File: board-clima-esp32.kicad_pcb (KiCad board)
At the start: 2 copper layers, 64.8 x 39.9 mm, 32 parts, among them IC1 ESP32-S3-WROOM-1-N4, J1 Conn_01x02_Pin, J2 Screw_Terminal_01x03, J3 Conn_01x04_Pin, J4 Conn_01x04_Pin, J5 Conn_01x04_Pin, J6 USB_C_Receptacle, Q1 AO3400A, SW1 RESET, SW2 BOOT, U1 AMS1117-3.3, U2 JZC-32F/C

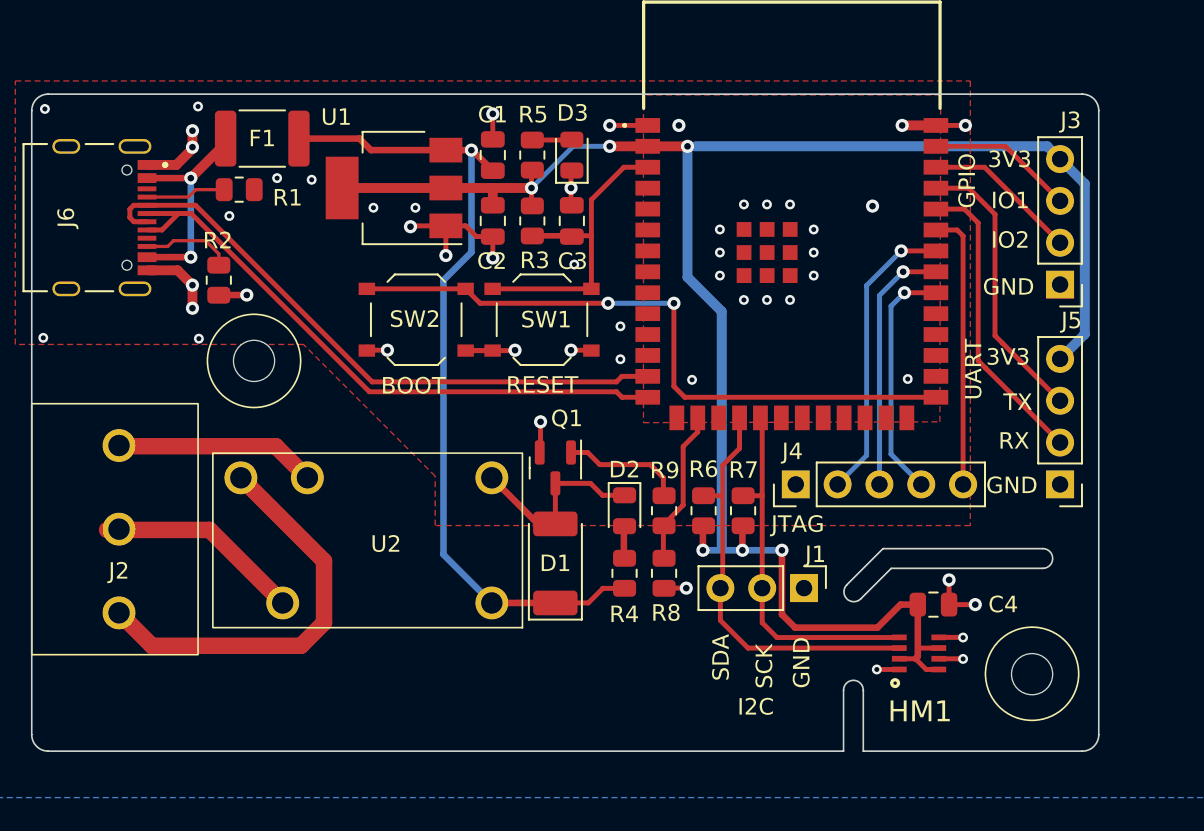
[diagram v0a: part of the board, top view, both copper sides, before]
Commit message: added bypass jumper
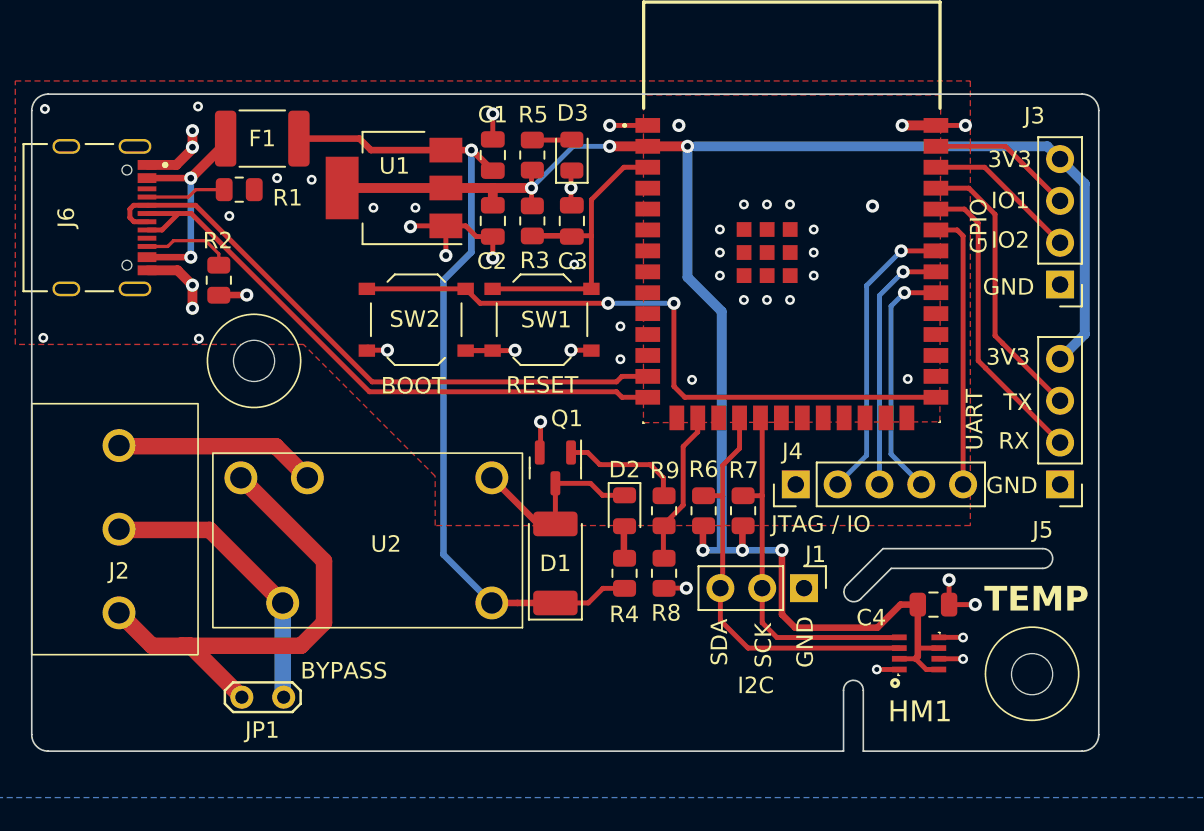
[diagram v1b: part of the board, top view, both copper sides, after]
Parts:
- added JP1: Jumper_2_Open, TestPoint:TestPoint_2Pads_Pitch2.54mm_Drill0.8mm, F.Cu at (106.3, 90.4)
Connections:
- net Net-(J2-Pin_1) renamed /R_NO
- net Net-(J2-Pin_2) renamed /R_COM
- J6 pad S1: unconnected-(J6-SHIELD-PadS1) -> GND
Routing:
- net /R_COM: track 12.5 -> 17.5 mm
- net /R_NO: track 24.8 -> 29.7 mm
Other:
- board text added: "BYPASS"
- board text added: "JTAG / IO"
- board text added: "TEMP"
- board text removed: "JTAG"

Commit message: pcb rev2 placement
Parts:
- removed J4: Conn_01x04_Pin, Connector_PinHeader_2.54mm:PinHeader_1x05_P2.54mm_Vertical
- added C5: 1u, Capacitor_SMD:C_0805_2012Metric, F.Cu at (159.8, 126.2)
- added D10: 15V, Diode_SMD:D_SOD-323, F.Cu at (169.2, 173.4)
- added D4: SM4007PL, Diode_SMD:D_SOD-123F, F.Cu at (160.0, 170.4)
- added D5: SM4007PL, Diode_SMD:D_SOD-123F, F.Cu at (163.3, 170.2)
- added D6: SM4007PL, Diode_SMD:D_SOD-123F, F.Cu at (160.0, 175.0)
- added D7: SM4007PL, Diode_SMD:D_SOD-123F, F.Cu at (163.3, 175.0)
- added D8: 4V3, Diode_SMD:D_SOD-323, F.Cu at (174.5, 176.5)
- added D9: 4V7, Diode_SMD:D_SOD-323, F.Cu at (169.2, 177.0)
- added H3: MountingHole, MountingHole:MountingHole_2.5mm, F.Cu at (130.3, 184.9)
- added H4: MountingHole, MountingHole:MountingHole_2.5mm, F.Cu at (200.7, 184.9)
- added Q2: AO3401A, Package_TO_SOT_SMD:SOT-23, F.Cu at (168.3, 169.9)
- added Q3: AO3400A, Package_TO_SOT_SMD:SOT-23, F.Cu at (165.6, 158.8)
- added R10: 10k, Resistor_SMD:R_0805_2012Metric, F.Cu at (170.2, 157.2)
- added R11: 330, Resistor_SMD:R_0805_2012Metric, F.Cu at (172.5, 169.2)
- added R12: 220, Resistor_SMD:R_0805_2012Metric, F.Cu at (166.9, 173.5)
- added R13: 100, Resistor_SMD:R_0805_2012Metric, F.Cu at (166.9, 177.0)
- added R14: 10k, Resistor_SMD:R_0805_2012Metric, F.Cu at (189.0, 179.1)
- added R15: 330, Resistor_SMD:R_0805_2012Metric, F.Cu at (189.0, 171.4)
- added R16: 220, Resistor_SMD:R_0805_2012Metric, F.Cu at (170.2, 165.4)
- added R17: 10k, Resistor_SMD:R_0805_2012Metric, F.Cu at (170.2, 163.1)
- added U3: PC817, Package_DIP:DIP-4_W7.62mm, F.Cu at (185.7, 172.2)
- added U4: PC817, Package_DIP:DIP-4_W7.62mm, F.Cu at (178.1, 176.5)
- D1: value SM4007 -> SM4007PL; footprint Diode_SMD:D_MELF -> Diode_SMD:D_SOD-123F
- D2: value LED -> SM4007PL; footprint LED_SMD:LED_0805_2012Metric -> Diode_SMD:D_SOD-123F
- J1: value Conn_01x02_Pin -> Conn_01x06_Pin; footprint Connector_PinHeader_2.54mm:PinHeader_1x03_P2.54mm_Vertical -> Connector_PinHeader_2.54mm:PinHeader_1x06_P2.54mm_Vertical
- J5: value Conn_01x04_Pin -> Conn_01x05_Pin; footprint Connector_PinHeader_2.54mm:PinHeader_1x04_P2.54mm_Vertical -> Connector_PinHeader_2.54mm:PinHeader_1x05_P2.54mm_Vertical
- R4: value 220 -> 0
- R5: value 220 -> 1k
- R8: value 10k -> 0
- U2: value JZC-32F/C -> ~; footprint JZC-32FC:JZC-32FC -> HFD2:HFD2-00X-M-L2
- moved C4 105.6 mm to (195.3, 178.1)
- moved J1 101.1 mm to (197.6, 165.4), turned to 180 degrees
- moved HM1 99.7 mm to (193.7, 176.2), turned to 90 degrees
- moved Q1 97.7 mm to (165.5, 164.3), turned to 180 degrees
- moved JP1 93.3 mm to (133.9, 179.6), turned to 90 degrees
- moved U2 90.9 mm to (157.1, 169.6)
- moved D1 90.3 mm to (160.4, 164.3), turned to -90 degrees
- moved R9 90.2 mm to (170.2, 159.5), turned to 0 degrees
- moved SW2 87.4 mm to (156.5, 144.1)
- moved R2 87.0 mm to (142.5, 142.2)
- moved D2 86.1 mm to (160.4, 158.5)
- moved J6 85.8 mm to (129.7, 138.9)
- moved R7 85.3 mm to (184.4, 148.1), turned to 0 degrees
- moved R6 84.9 mm to (184.4, 145.8), turned to 0 degrees
- moved R1 84.9 mm to (138.2, 137.2)
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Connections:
- D1 pad 1: +5V -> Net-(D1-K)
- D2 pad 1: Net-(D1-A) -> Net-(D2-K)
- IC1 pad 16: /RELAY -> unconnected-(IC1-IO46-Pad16)
- IC1 pad 18: /SDA -> /BOILER_1
- IC1 pad 19: /SCK -> /BOILER_2
- IC1 pad 21: unconnected-(IC1-IO13-Pad21) -> /GPIO4
- IC1 pad 22: unconnected-(IC1-IO14-Pad22) -> /GPIO5
- IC1 pad 23: unconnected-(IC1-IO21-Pad23) -> /SDA
- IC1 pad 24: unconnected-(IC1-IO47-Pad24) -> /SCK
- IC1 pad 31: unconnected-(IC1-IO38-Pad31) -> /GPIO3
- IC1 pad 32: /JTAG_TCK -> unconnected-(IC1-IO39-Pad32)
- IC1 pad 33: /JTAG_TDO -> unconnected-(IC1-IO40-Pad33)
- IC1 pad 34: /JTAG_TDI -> unconnected-(IC1-IO41-Pad34)
- IC1 pad 35: /JTAG_TMS -> unconnected-(IC1-IO42-Pad35)
- IC1 pad 38: /GPIO2 -> /GPIO1
- IC1 pad 39: /GPIO1 -> /GPIO2
- J1 pad 1: GND -> /GPIO5
- J1 pad 2: /SCK -> /GPIO4
- J2 pad 3: Net-(J2-Pin_3) -> /R_NC
- J5 pad 1: GND -> /GPIO3
- J5 pad 4: +3.3V -> GND
- R4 pad 2: Net-(D2-A) -> Net-(D1-K)
- R6 pad 2: /SDA -> /SCK
- R7 pad 2: /SCK -> /SDA
- R8 pad 1: /RELAY -> +5V
- R8 pad 2: GND -> Net-(D2-K)
- R9 pad 1: /RELAY -> /BOILER_2
- R9 pad 2: Net-(Q1-G) -> Net-(Q3-G)
- U2 pad 1: +5V -> Net-(D1-A)
- U2 pad 2: Net-(D1-A) -> Net-(D2-A)
- U2 pad 4: Net-(J2-Pin_3) -> /R_COM
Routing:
- net +3.3V: track 114.0 -> 0.00 mm, vias 6 -> 0
- net +5V: track 50.4 -> 0.00 mm, vias 1 -> 0
- net GND: track 46.3 -> 0.00 mm, vias 51 -> 0
- net /BOOT: track 39.8 -> 0.00 mm, vias 2 -> 0
- net /USB-: track 37.4 -> 0.00 mm
- net /USB+: track 36.8 -> 0.00 mm
- net /R_NO: track 29.7 -> 0.00 mm
- net /SDA: track 25.1 -> 0.00 mm
- net /SCK: track 22.5 -> 0.00 mm
- net Net-(IC1-EN): track 21.2 -> 0.00 mm
- net /UART_RX: track 18.8 -> 0.00 mm
- net /JTAG_TDI: track 17.9 -> 0.00 mm, vias 1 -> 0
- net /UART_TX: track 17.6 -> 0.00 mm
- net /R_COM: track 17.5 -> 0.00 mm
- net /JTAG_TMS: track 17.3 -> 0.00 mm
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- removed copper zone on B.Cu, net GND
- removed copper zone on F.Cu, net GND
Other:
- board size 64.8 x 39.9 mm -> 76.2 x 64.3 mm
- board text removed: "${COMMENT1}"
- board text removed: "${COMPANY} ${REVISION} NO WARRANTY WHATSOEVER USAGE AT USER'S OWN RISK"
- board text removed: "3V3"
- board text removed: "BOOT"
- board text removed: "BYPASS"
- board text removed: "GND"
- board text removed: "GPIO"
- board text removed: "I2C"
- board text removed: "IO1"
- board text removed: "IO2"
- board text removed: "JTAG / IO"
- board text removed: "RESET"
- board text removed: "RX"
- board text removed: "SCK"
- board text removed: "SDA"
- board text removed: "TEMP"
- board text removed: "TX"
- board text removed: "UART"

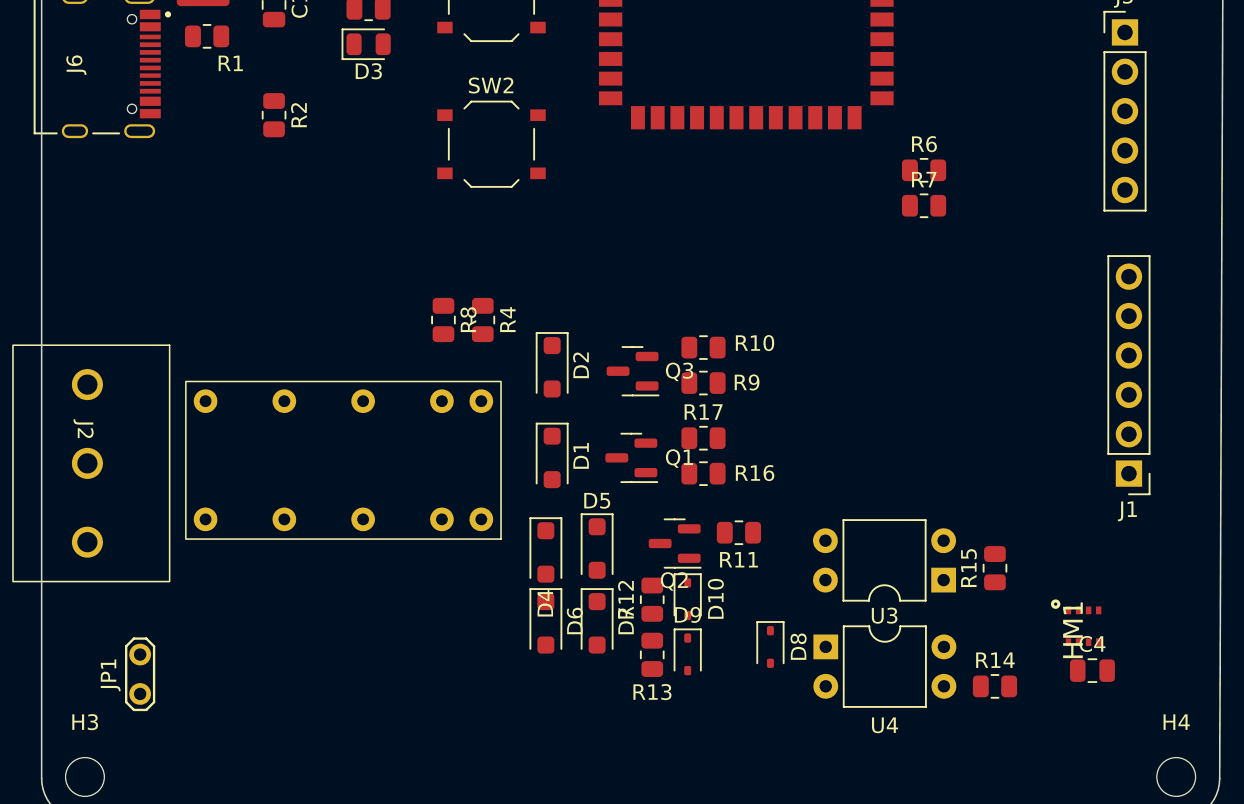
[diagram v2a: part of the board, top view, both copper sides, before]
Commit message: New J1 connector location
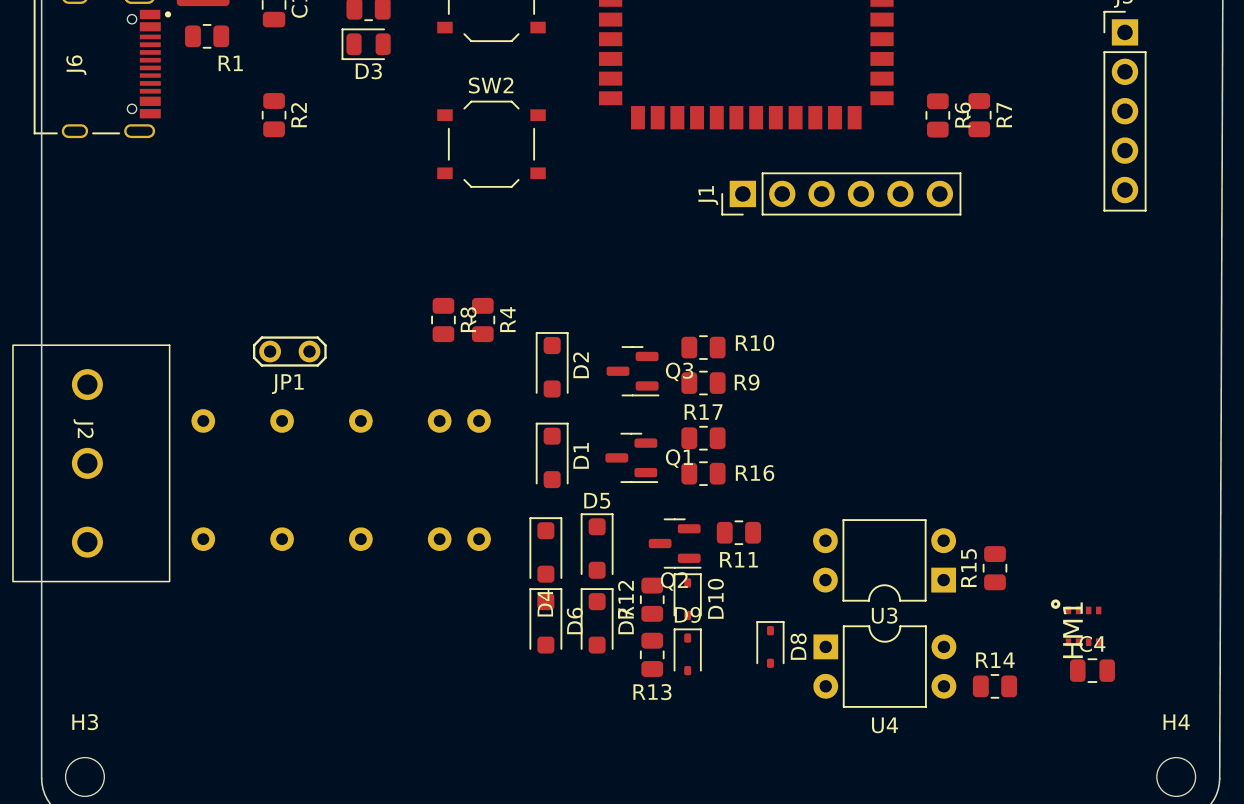
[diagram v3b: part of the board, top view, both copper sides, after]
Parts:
- U2: moved to B.Cu
- moved J1 30.7 mm to (172.7, 147.3), turned to 90 degrees
- moved JP1 24.6 mm to (144.8, 157.5), turned to 180 degrees
- moved U2 8.89 mm to (157.0, 160.7)
- moved R7 6.84 mm to (188.0, 142.2), turned to -90 degrees
- moved R6 3.65 mm to (185.3, 142.3), turned to -90 degrees
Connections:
- J1 pad 1: /GPIO5 -> /GPIO4
- J1 pad 2: /GPIO4 -> /GPIO5
- J1 pad 3: /SDA -> /SCK
- J1 pad 4: /SCK -> /SDA

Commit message: Cleanup pcb layout for easier routing
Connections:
- net /GPIO4 renamed /DISP_BUSY
- net /GPIO5 renamed /DISP_RST
- IC1 pad 23: /SDA -> /SCK
- IC1 pad 24: /SCK -> /SDA
- J5 pad 1: /GPIO3 -> GND
- J5 pad 4: GND -> /GPIO3
- R6 pad 2: /SCK -> /SDA
- R7 pad 2: /SDA -> /SCK
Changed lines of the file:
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@@
   (net 30 "unconnected-(IC1-IO46-Pad16)")
   (net 31 "unconnected-(IC1-IO9-Pad17)")
-  (net 32 "/GPIO4")
-  (net 33 "/GPIO5")
+  (net 32 "/DISP_RST")
+  (net 33 "/DISP_BUSY")
   (net 34 "unconnected-(IC1-IO12-Pad20)")
   (net 35 "/BOILER_1")
@@
       (net 34 "unconnected-(IC1-IO12-Pad20)") (pinfunction "IO12") (pintype "passive+no_connect"))
     (pad "21" smd rect (at 0.635 12.5) (size 0.9 1.5) (layers "F.Cu" "F.Paste" "F.Mask")
-      (net 32 "/GPIO4") (pinfunction "IO13") (pintype "passive"))
+      (net 33 "/DISP_BUSY") (pinfunction "IO13") (pintype "passive"))
     (pad "22" smd rect (at 1.905 12.5) (size 0.9 1.5) (layers "F.Cu" "F.Paste" "F.Mask")
-      (net 33 "/GPIO5") (pinfunction "IO14") (pintype "passive"))
+      (net 32 "/DISP_RST") (pinfunction "IO14") (pintype "passive"))
     (pad "23" smd rect (at 3.175 12.5) (size 0.9 1.5) (layers "F.Cu" "F.Paste" "F.Mask")
-      (net 16 "/SDA") (pinfunction "IO21") (pintype "passive"))
+      (net 17 "/SCK") (pinfunction "IO21") (pintype "passive"))
     (pad "24" smd rect (at 4.445 12.5) (size 0.9 1.5) (layers "F.Cu" "F.Paste" "F.Mask")
-      (net 17 "/SCK") (pinfunction "IO47") (pintype "passive"))
+      (net 16 "/SDA") (pinfunction "IO47") (pintype "passive"))
     (pad "25" smd rect (at 5.715 12.5) (size 0.9 1.5) (layers "F.Cu" "F.Paste" "F.Mask")
       (net 37 "unconnected-(IC1-IO48-Pad25)") (pinfunction "IO48") (pintype "passive+no_connect"))
@@
       (net 3 "+3.3V") (pintype "passive"))
     (pad "2" smd roundrect (at 0.9125 0 270) (size 1.025 1.4) (layers "F.Cu" "F.Paste" "F.Mask") (roundrect_rratio 0.243902)
-      (net 16 "/SDA") (pintype "passive"))
+      (net 17 "/SCK") (pintype "passive"))
     (model "${KICAD6_3DMODEL_DIR}/Resistor_SMD.3dshapes/R_0805_2012Metric.wrl"
       (offset (xyz 0 0 0))
@@
       (stroke (width 0.1) (type solid)) (layer "F.Fab"))
     (pad "1" thru_hole rect (at 0 0 90) (size 1.7 1.7) (drill 1) (layers "*.Cu" "*.Mask")
-      (net 32 "/GPIO4") (pinfunction "Pin_1") (pintype "passive"))
+      (net 33 "/DISP_BUSY") (pinfunction "Pin_1") (pintype "passive"))
     (pad "2" thru_hole oval (at 0 2.54 90) (size 1.7 1.7) (drill 1) (layers "*.Cu" "*.Mask")
-      (net 33 "/GPIO5") (pinfunction "Pin_2") (pintype "passive"))
+      (net 32 "/DISP_RST") (pinfunction "Pin_2") (pintype "passive"))
     (pad "3" thru_hole oval (at 0 5.08 90) (size 1.7 1.7) (drill 1) (layers "*.Cu" "*.Mask")
       (net 17 "/SCK") (pinfunction "Pin_3") (pintype "passive"))
@@
       (stroke (width 0.1) (type solid)) (layer "F.Fab"))
     (pad "1" thru_hole rect (at 0 0) (size 1.7 1.7) (drill 1) (layers "*.Cu" "*.Mask")
-      (net 43 "/GPIO3") (pinfunction "Pin_1") (pintype "passive"))
+      (net 2 "GND") (pinfunction "Pin_1") (pintype "passive"))
     (pad "2" thru_hole oval (at 0 2.54) (size 1.7 1.7) (drill 1) (layers "*.Cu" "*.Mask")
       (net 51 "/GPIO2") (pinfunction "Pin_2") (pintype "passive"))
@@
       (net 50 "/GPIO1") (pinfunction "Pin_3") (pintype "passive"))
     (pad "4" thru_hole oval (at 0 7.62) (size 1.7 1.7) (drill 1) (layers "*.Cu" "*.Mask")
-      (net 2 "GND") (pinfunction "Pin_4") (pintype "passive"))
+      (net 43 "/GPIO3") (pinfunction "Pin_4") (pintype "passive"))
     (pad "5" thru_hole oval (at 0 10.16) (size 1.7 1.7) (drill 1) (layers "*.Cu" "*.Mask")
       (net 3 "+3.3V") (pinfunction "Pin_5") (pintype "passive"))
@@
       (net 3 "+3.3V") (pintype "passive"))
     (pad "2" smd roundrect (at 0.9125 0 270) (size 1.025 1.4) (layers "F.Cu" "F.Paste" "F.Mask") (roundrect_rratio 0.243902)
-      (net 17 "/SCK") (pintype "passive"))
+      (net 16 "/SDA") (pintype "passive"))
     (model "${KICAD6_3DMODEL_DIR}/Resistor_SMD.3dshapes/R_0805_2012Metric.wrl"
       (offset (xyz 0 0 0))

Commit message: rev2 routing
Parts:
- moved R15 29.6 mm to (169.2, 149.5)
- moved R14 28.0 mm to (177.8, 153.4)
- moved U3 22.5 mm to (169.2, 157.0), turned to -90 degrees
- moved U2 20.7 mm to (137.2, 154.7), turned to -90 degrees
- moved D1 19.8 mm to (144.3, 152.9), turned to 0 degrees
- moved R17 19.7 mm to (154.1, 151.6)
- moved R16 19.5 mm to (154.1, 154.4)
- moved Q1 19.0 mm to (149.8, 153.7)
- moved R8 15.8 mm to (138.2, 151.4)
- moved R4 15.8 mm to (140.7, 151.4)
- moved R11 15.0 mm to (158.2, 164.3)
- moved J3 14.9 mm to (199.1, 139.4), turned to 180 degrees
- moved D9 13.1 mm to (156.5, 174.0)
- moved U4 12.7 mm to (173.7, 164.6), turned to 90 degrees
- moved JP1 11.8 mm to (133.3, 154.7)
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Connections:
- U2 pad 1: Net-(D1-A) -> Net-(D1-K)
- U2 pad 11: unconnected-(U2-NC2-Pad11) -> /R_NC
- U2 pad 13: unconnected-(U2-CM2-Pad13) -> /R_COM
- U2 pad 15: Net-(D2-K) -> Net-(D2-A)
- U2 pad 16: Net-(D1-K) -> Net-(D1-A)
- U2 pad 2: Net-(D2-A) -> Net-(D2-K)
- U2 pad 4: /R_COM -> unconnected-(U2-CM1-Pad4)
- U2 pad 6: /R_NC -> unconnected-(U2-NC1-Pad6)
- U2 pad 8: /R_NO -> unconnected-(U2-NO1-Pad8)
- U2 pad 9: unconnected-(U2-NO2-Pad9) -> /R_NO
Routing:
- net +3.3V: track 0.00 -> 167.2 mm, vias 0 -> 3
- net GND: track 0.00 -> 86.8 mm, vias 0 -> 26
- net /OT_COM: track 0.00 -> 48.8 mm
- net /SCK: track 0.00 -> 46.1 mm, vias 0 -> 1
- net /BOILER_2: track 0.00 -> 41.1 mm
- net /SDA: track 0.00 -> 40.5 mm
- net /R_COM: track 0.00 -> 33.8 mm
- net /R_NO: track 0.00 -> 33.8 mm
- net /USB-: track 0.00 -> 33.8 mm
- net /USB+: track 0.00 -> 33.0 mm
- net +5V: track 0.00 -> 32.2 mm, vias 0 -> 2
- net /GPIO1: track 0.00 -> 30.0 mm, vias 0 -> 1
- net /BOOT: track 0.00 -> 29.6 mm, vias 0 -> 2
- net /GPIO2: track 0.00 -> 28.9 mm, vias 0 -> 1
- net Net-(IC1-EN): track 0.00 -> 26.1 mm
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- added copper zone on B.Cu, net GND
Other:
- outline, holes or cut-outs redrawn

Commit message: silkscreen
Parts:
- moved J5 10.2 mm to (199.1, 154.4), turned to 180 degrees
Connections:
- J5 pad 1: GND -> /GPIO3
- J5 pad 4: /GPIO3 -> GND
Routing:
- net /GPIO2: track 28.9 -> 43.4 mm, vias 1 -> 0
- net +3.3V: track 167.2 -> 158.2 mm
- net Net-(F1-Pad1): track 6.45 -> 11.8 mm
- net /GPIO3: track 25.8 -> 28.0 mm
- net /GPIO1: track 30.0 -> 30.6 mm, vias 1 -> 2
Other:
- board text added: "3V3"
- board text added: "BME280"
- board text added: "BOARD VARIANT [ ] RELAY [ ] OPENTHERM [ ] BME280 RELAY/OPENTHERM VARIANTS ARE MUTUALLY EXCLUSIVE DON'T MOUNT BOTH AT THE SAME TIME!"
- board text added: "COM/ OT2"
- board text added: "EDOARDO FULLIN REV2 202401 NO WARRANTY WHATSOEVER USAGE AT USER'S OWN RISK"
- board text added: "ESP32-S3 VERSION"
- board text added: "GND"
- board text added: "GPIO"
- board text added: "I2C DISP"
- board text added: "IO1"
- board text added: "IO13"
- board text added: "IO14"
- board text added: "IO2"
- board text added: "IO38"
- board text added: "NC"
- board text added: "NO/ OT1"
- board text added: "ON/OFF RELAY"
- board text added: "OPENTHERM"
- board text added: "RX"
- board text added: "SCK"
- board text added: "SDA"
- board text added: "TX"
- board text added: "UART"
